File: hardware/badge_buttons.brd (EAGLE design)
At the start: 86.8 x 58.3 mm, 7 parts, among them U2 MLX90614

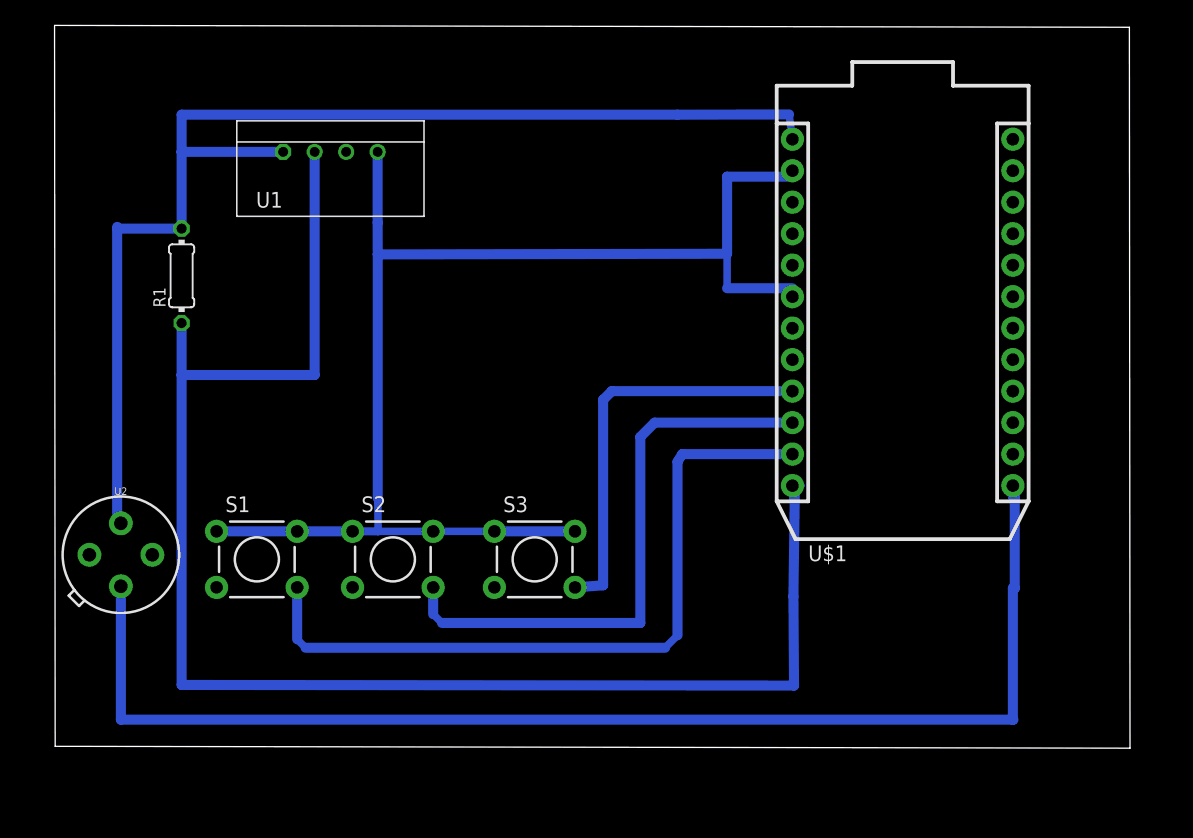
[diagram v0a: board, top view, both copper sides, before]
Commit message: refactor directory/finish wiring
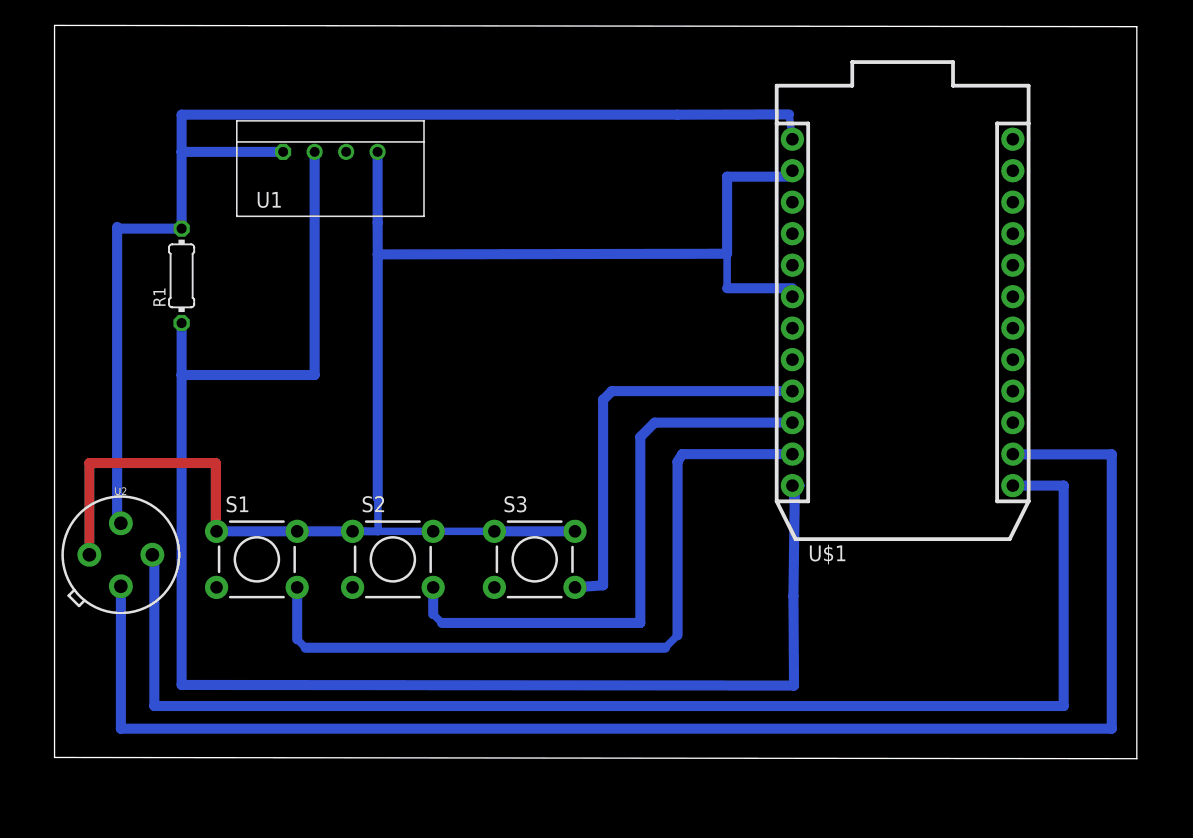
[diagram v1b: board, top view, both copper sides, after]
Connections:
- new net N$8: U$1.14, U2.1
- net N$7: now also U2.2; no longer U2.1
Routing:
- net N$8: track 0.00 -> 121.5 mm
- net N$4: track 110.4 -> 133.5 mm
- net N$7: track 101.9 -> 107.6 mm
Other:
- board size 86.8 x 58.3 mm -> 87.3 x 59.2 mm
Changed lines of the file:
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@@
 <board>
 <plain>
-<wire x1="5.8" y1="10.05" x2="92.5" y2="9.9" width="0" layer="20"/>
-<wire x1="92.5" y1="9.9" x2="92.45" y2="68.05" width="0" layer="20"/>
-<wire x1="92.45" y1="68.05" x2="5.75" y2="68.2" width="0" layer="20"/>
-<wire x1="5.75" y1="68.2" x2="5.8" y2="10.05" width="0" layer="20"/>
+<wire x1="5.75" y1="9.15" x2="93.05" y2="9.05" width="0" layer="20"/>
+<wire x1="93.05" y1="9.05" x2="93.05" y2="68.1" width="0" layer="20"/>
+<wire x1="93.05" y1="68.1" x2="5.75" y2="68.2" width="0" layer="20"/>
+<wire x1="5.75" y1="68.2" x2="5.75" y2="9.15" width="0" layer="20"/>
 </plain>
 <attributes>
@@
 <wire x1="60" y1="56" x2="60" y2="49.78" width="0.8128" layer="16"/>
 <contactref element="U2" pad="4"/>
-<wire x1="8.56" y1="25.5" x2="18.8188" y2="27.3906" width="0" layer="19" extent="1-1"/>
+<wire x1="8.56" y1="25.5" x2="8.56" y2="32.9" width="0.8128" layer="1"/>
+<wire x1="8.56" y1="32.9" x2="18.75" y2="32.9" width="0.8128" layer="1"/>
+<wire x1="18.75" y1="32.9" x2="18.75" y2="27.3906" width="0.8128" layer="1"/>
+<wire x1="18.75" y1="27.3906" x2="18.8188" y2="27.3906" width="0.8128" layer="1"/>
 </signal>
 <signal name="N$5">
@@
 </signal>
 <signal name="N$7">
+<contactref element="U2" pad="2"/>
+<contactref element="U$1" pad="13"/>
+<wire x1="13.64" y1="25.5" x2="13.8" y2="25.5" width="0.8128" layer="16"/>
+<wire x1="13.8" y1="25.5" x2="13.8" y2="13.3" width="0.8128" layer="16"/>
+<wire x1="13.8" y1="13.3" x2="87.15" y2="13.3" width="0.8128" layer="16"/>
+<wire x1="87.15" y1="31.08" x2="83.05" y2="31.08" width="0.8128" layer="16"/>
+<wire x1="87.15" y1="13.3" x2="87.15" y2="31.08" width="0.8128" layer="16"/>
+</signal>
+<signal name="N$8">
 <contactref element="U2" pad="1"/>
-<contactref element="U$1" pad="13"/>
-<wire x1="11.1" y1="22.96" x2="11.1" y2="12.2" width="0.8128" layer="16"/>
-<wire x1="11.1" y1="12.2" x2="83.05" y2="12.2" width="0.8128" layer="16"/>
-<wire x1="83.1" y1="12.2" x2="83.05" y2="12.2" width="0.8128" layer="16"/>
-<wire x1="83.05" y1="12.2" x2="83.05" y2="22.7996" width="0.8128" layer="16"/>
-<wire x1="83.05" y1="22.7996" x2="83.2024" y2="22.7996" width="0.8128" layer="16"/>
-<wire x1="83.2024" y1="22.7996" x2="83.2024" y2="30.2164" width="0.8128" layer="16"/>
-<wire x1="83.2024" y1="30.2164" x2="83.05" y2="30.2164" width="0.8128" layer="16"/>
-<wire x1="83.05" y1="30.2164" x2="83.05" y2="31.08" width="0.8128" layer="16"/>
+<contactref element="U$1" pad="14"/>
+<wire x1="11.1" y1="22.96" x2="11.1" y2="11.4724" width="0.8128" layer="16"/>
+<wire x1="91.0276" y1="11.4724" x2="91.0276" y2="33.6" width="0.8128" layer="16"/>
+<wire x1="11.1" y1="11.4724" x2="91.0276" y2="11.4724" width="0.8128" layer="16"/>
+<wire x1="91.0276" y1="33.6" x2="83.05" y2="33.6" width="0.8128" layer="16"/>
+<wire x1="83.05" y1="33.6" x2="83.05" y2="33.62" width="0.8128" layer="16"/>
 </signal>
 </signals>

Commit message: last add
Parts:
- moved U1 12.5 mm to (28.0, 45.5)
- moved S3 0.95 mm to (43.5, 25.1)
- moved R1 0.30 mm to (16.0, 47.7)
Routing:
- net N$6: track 127.1 -> 114.3 mm
- net N$5: track 97.8 -> 107.6 mm
- net N$4: track 133.5 -> 128.4 mm
- net N$1: track 33.2 -> 34.4 mm
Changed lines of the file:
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@@
 <element name="S1" library="SparkFun-Retired" package="TACTILE-PTH" value="" x="22.07" y="25.13"/>
 <element name="S2" library="SparkFun-Retired" package="TACTILE-PTH" value="" x="33.04" y="25.13"/>
-<element name="S3" library="SparkFun-Retired" package="TACTILE-PTH" value="" x="44.48" y="25.13"/>
+<element name="S3" library="SparkFun-Retired" package="TACTILE-PTH" value="" x="43.53" y="25.13"/>
 <element name="U$1" library="Particle-Devices" package="PHOTON" value="PHOTON_WITH_HEADERS" x="64" y="26"/>
-<element name="U1" library="RHT03_DHT-22_AM2302" package="RHT03_DHT-22" value="" x="28" y="58">
-<attribute name="PROD_ID" value="SEN-10167" x="28" y="58" size="1.778" layer="27" display="off"/>
+<element name="U1" library="RHT03_DHT-22_AM2302" package="RHT03_DHT-22" value="" x="28" y="45.45">
+<attribute name="PROD_ID" value="SEN-10167" x="28" y="45.45" size="1.778" layer="27" display="off"/>
 </element>
-<element name="R1" library="resistor" library_urn="urn:adsk.eagle:library:348" package="0204/7" package3d_urn="urn:adsk.eagle:package:25945/1" value="" x="16" y="48" rot="R90"/>
+<element name="R1" library="resistor" library_urn="urn:adsk.eagle:library:348" package="0204/7" package3d_urn="urn:adsk.eagle:package:25945/1" value="" x="16" y="47.7" rot="R90"/>
 <element name="U2" library="SparkFun-Sensors" package="TO-39" value="MLX90614" x="11.1" y="25.5" rot="R270">
 <attribute name="PROD_ID" value="COMP-09719" x="11.1" y="25.5" size="1.778" layer="27" rot="R270" display="off"/>
@@
 <wire x1="65.27" y1="38.7" x2="65" y2="38.97" width="0.3048" layer="16"/>
 <wire x1="65" y1="38.97" x2="65" y2="39" width="0.3048" layer="16"/>
-<wire x1="47.7312" y1="22.8694" x2="50" y2="23.0382" width="0.8128" layer="16"/>
-<wire x1="50" y1="23.0382" x2="50" y2="38" width="0.8128" layer="16"/>
+<wire x1="46.7812" y1="22.8694" x2="50" y2="22.8382" width="0.8128" layer="16"/>
+<wire x1="50" y1="22.8382" x2="50" y2="38" width="0.8128" layer="16"/>
 <wire x1="50" y1="38" x2="50.7" y2="38.7" width="0.8128" layer="16"/>
 <wire x1="50.7" y1="38.7" x2="65.27" y2="38.7" width="0.8128" layer="16"/>
@@
 <wire x1="36.4" y1="27.3" x2="36.3906" y2="27.3906" width="0.508" layer="16"/>
 <wire x1="36.2912" y1="27.3906" x2="36.3906" y2="27.3906" width="0.6096" layer="16"/>
-<wire x1="36.3906" y1="27.3906" x2="41.2288" y2="27.3906" width="0.6096" layer="16"/>
-<wire x1="41.2288" y1="27.3906" x2="47.7312" y2="27.3906" width="0.8128" layer="16"/>
-<wire x1="31.81" y1="58" x2="31.81" y2="52.29" width="0.8128" layer="16"/>
-<wire x1="31.81" y1="52.29" x2="31.82" y2="49.73" width="0.8128" layer="16"/>
-<wire x1="31.82" y1="49.73" x2="31.82" y2="30.0606" width="0.8128" layer="16"/>
+<wire x1="36.3906" y1="27.3906" x2="40.2788" y2="27.3906" width="0.6096" layer="16"/>
+<wire x1="40.2788" y1="27.3906" x2="46.7812" y2="27.3906" width="0.8128" layer="16"/>
+<wire x1="31.81" y1="45.45" x2="31.76" y2="48.99" width="0.8128" layer="16"/>
+<wire x1="31.76" y1="48.99" x2="31.92" y2="49.68" width="0.8128" layer="16"/>
+<wire x1="31.92" y1="49.68" x2="31.82" y2="30.0606" width="0.8128" layer="16"/>
 <wire x1="31.82" y1="30.0606" x2="31.85305" y2="27.371971875" width="0.6096" layer="16"/>
 <contactref element="U$1" pad="6"/>
 <wire x1="31.85305" y1="27.371971875" x2="30" y2="27.3906" width="0.6096" layer="16"/>
-<wire x1="60" y1="49.78" x2="31.82" y2="49.73" width="0.8128" layer="16"/>
+<wire x1="60" y1="49.78" x2="31.92" y2="49.68" width="0.8128" layer="16"/>
 <wire x1="65.27" y1="46.32" x2="65.27" y2="47" width="0.508" layer="16"/>
 <wire x1="65.27" y1="47" x2="60" y2="47" width="0.8128" layer="16"/>
@@
 <contactref element="U$1" pad="1"/>
 <contactref element="R1" pad="2"/>
-<wire x1="24.19" y1="58" x2="16" y2="58" width="0.8128" layer="16"/>
-<wire x1="16" y1="58" x2="16" y2="61" width="0.8128" layer="16"/>
-<wire x1="16" y1="61" x2="56" y2="61" width="0.8128" layer="16"/>
+<wire x1="24.19" y1="45.45" x2="16.5" y2="61.55" width="0.8128" layer="16"/>
+<wire x1="16.5" y1="61.55" x2="19.6" y2="61.5" width="0.8128" layer="16"/>
+<wire x1="19.6" y1="61.5" x2="56" y2="61" width="0.8128" layer="16"/>
 <wire x1="56" y1="61" x2="65" y2="61.02" width="0.8128" layer="16"/>
 <wire x1="65" y1="61.02" x2="65.27" y2="59.02" width="0.6096" layer="16"/>
-<wire x1="16" y1="58" x2="16" y2="51.81" width="0.8128" layer="16"/>
+<wire x1="16.5" y1="61.55" x2="16" y2="51.51" width="0.8128" layer="16"/>
 <contactref element="U2" pad="3"/>
-<wire x1="16" y1="51.81" x2="10.8" y2="51.81" width="0.8128" layer="16"/>
-<wire x1="10.8" y1="51.81" x2="10.8" y2="51.95" width="0.8128" layer="16"/>
-<wire x1="10.8" y1="51.81" x2="10.8" y2="28.04" width="0.8128" layer="16"/>
+<wire x1="16" y1="51.51" x2="10.85" y2="51.41" width="0.8128" layer="16"/>
+<wire x1="10.85" y1="51.41" x2="10.8" y2="51.8" width="0.8128" layer="16"/>
+<wire x1="10.85" y1="51.41" x2="10.8" y2="28.04" width="0.8128" layer="16"/>
 <wire x1="10.8" y1="28.04" x2="11.1" y2="28.04" width="0.8128" layer="16"/>
 </signal>
@@
 <contactref element="U$1" pad="12"/>
 <contactref element="R1" pad="1"/>
-<wire x1="26.73" y1="58" x2="26.73" y2="40" width="0.8128" layer="16"/>
+<wire x1="26.73" y1="45.45" x2="26.73" y2="40" width="0.8128" layer="16"/>
 <wire x1="26.73" y1="40" x2="16" y2="40" width="0.8128" layer="16"/>
 <wire x1="16" y1="40" x2="16" y2="15" width="0.8128" layer="16"/>
@@
 <wire x1="65.27" y1="30.064" x2="65.15" y2="30.964" width="0.508" layer="16"/>
 <wire x1="65.15" y1="30.964" x2="66" y2="31.08" width="0.508" layer="16"/>
-<wire x1="16" y1="44.19" x2="16" y2="40" width="0.8128" layer="16"/>
+<wire x1="16" y1="43.89" x2="16" y2="40" width="0.8128" layer="16"/>
 </signal>
 <signal name="N$7">

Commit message: pusher T
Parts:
- removed U2: MLX90614, SparkFun-Sensors:TO-39
- added JP1: (no value), jumper:JP4
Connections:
- new net N$10: JP1.1, U$1.16
- new net N$9: JP1.2, U$1.15
- net N$4: no longer U2.4
- net N$5: no longer U2.3
- net N$7: now also JP1.4; no longer U2.2
- net N$8: now also JP1.3; no longer U2.1
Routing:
- net N$10: track 0.00 -> 133.5 mm
- net N$9: track 0.00 -> 121.2 mm
- net N$5: track 107.6 -> 63.0 mm
- net N$4: track 128.4 -> 105.3 mm
- net N$7: track 107.6 -> 94.3 mm
- net N$8: track 121.5 -> 109.4 mm
- net N$3: track 59.2 -> 61.7 mm
- net N$2: track 46.9 -> 49.1 mm
- net N$6: track 114.3 -> 113.4 mm
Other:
- board size 87.3 x 59.2 mm -> 92.2 x 63.6 mm
- board text added: "Vin"
